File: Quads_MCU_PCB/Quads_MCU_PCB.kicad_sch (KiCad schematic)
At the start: 87 parts, among them J1 USB_C_Receptacle_USB2.0_16P, J2 Conn_01x06_Pin, J3 Conn_01x02_Pin, J4 Conn_01x03_Pin, J5 Conn_01x03_Pin, J6 Conn_01x03_Pin, J7 Conn_01x03_Pin, SW1 SW_Push, U1 STM32H723ZGTx, U3 ISOW1044, U4 TSR_1-2450, U5 AP7361C-33E, U6 ISOW1044, U7 ISOW1044, U8 MCP2518FD-xQBB, U9 ISOW1044, Y1 40MHz, Y2 25MHz

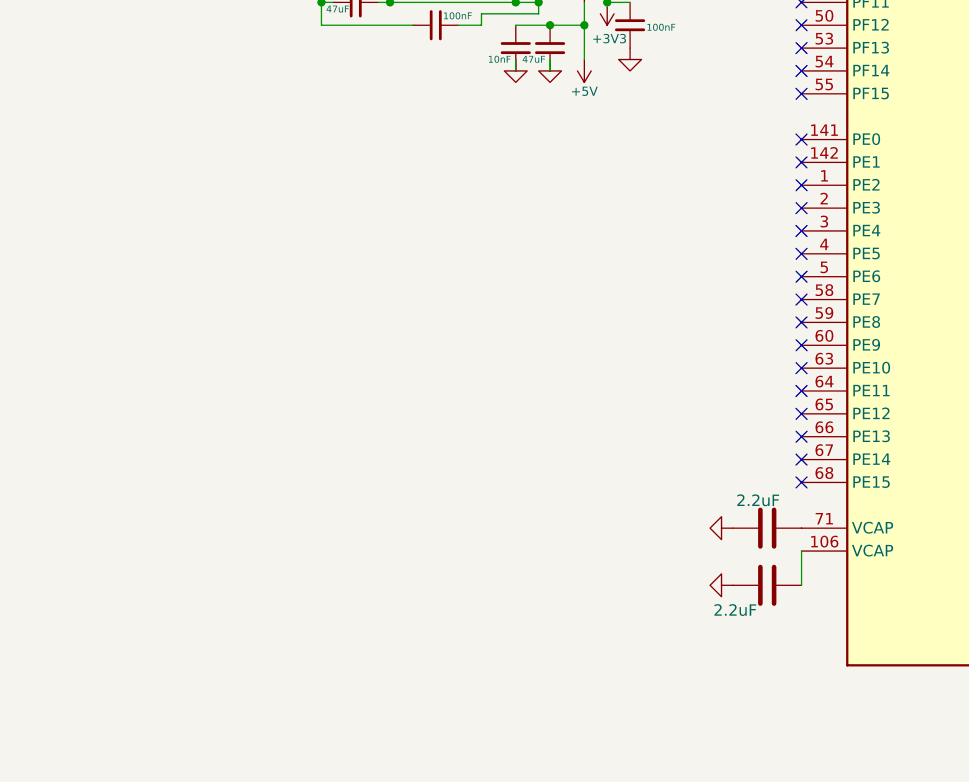
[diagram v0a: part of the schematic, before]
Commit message: Add BMI088 IMU on SPI4
U10 BMI088 (Sensor_Motion:BMI088, Bosch LGA-16) wired per datasheet
Fig. 8 (SPI mode):
- SPI4: PE2 SCK, PE5 MISO (SDO1 + SDO2), PE6 MOSI
- Chip selects as GPIO: PE3 -> CSB1 (accel), PE4 -> CSB2 (gyro)
- Data-ready interrupts: PE7 <- INT1 (accel), PE8 <- INT3 (gyro)
- PS tied to GND (selects SPI); INT2/INT4 left unconnected
- C59/C60 100nF decoupling on VDD/VDDIO, both from +3V3
- Removed the no-connect flags on PE2-PE8

SPI4 is separate from SPI1 so IMU reads don't compete with MCP2518FD
CAN traffic. ERC adds one expected pin_to_pin error: SDO1/SDO2 are both
"output" but tri-state when their CS is high, as in Bosch Fig. 8.

Co-Authored-By: Claude Opus 5.5 <noreply@anthropic.com>
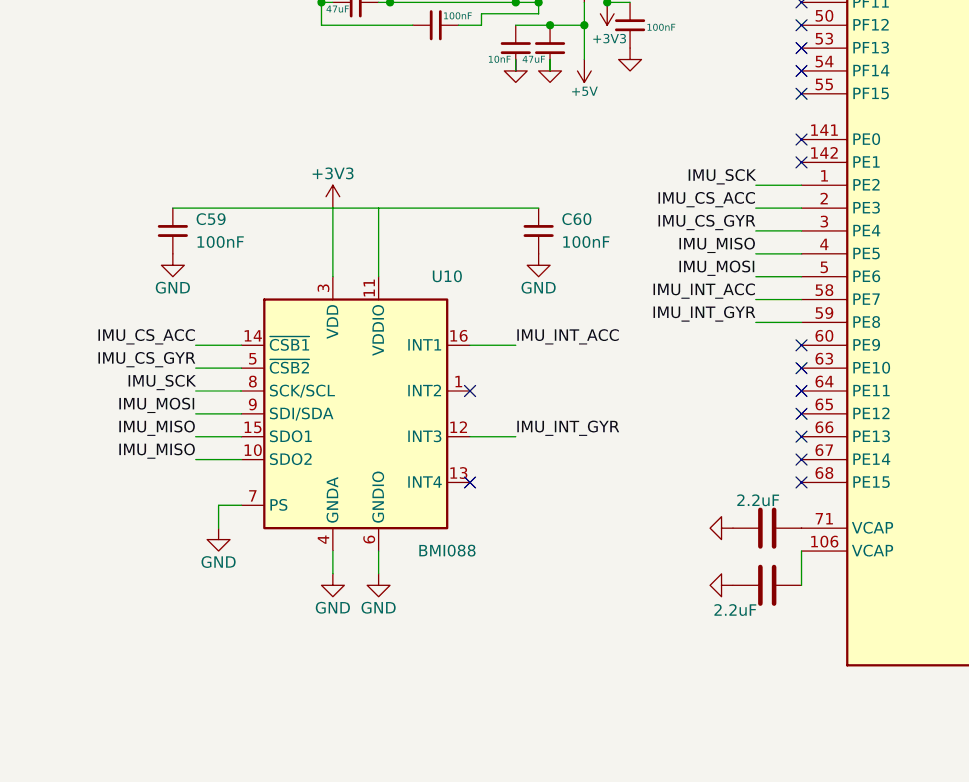
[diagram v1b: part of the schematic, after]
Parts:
- added C59, C60: 100nF, Capacitor_SMD:C_0402_1005Metric, symbol Device:C_Small
- added U10: BMI088, Package_LGA:Bosch_LGA-16_4.5x3mm_P0.5mm_LayoutBorder7x1y_ClockwisePinNumbering, symbol Sensor_Motion:BMI088
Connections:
- net +3V3: now also C59.1, C60.1, U10.11 (VDDIO), U10.3 (VDD)
- net GND: now also C59.2, C60.2, U10.2 (GNDA), U10.4 (GNDA), U10.6 (GNDIO), U10.7 (PS)
- net IMU_SCK: now reaches U1.1 (PE2)
- net IMU_SCK: now also U10.8 (SCK/SCL)
- net IMU_CS_ACC: now reaches U1.2 (PE3)
- net IMU_CS_ACC: now also U10.14 (~{CSB1})
- net IMU_CS_GYR: now reaches U1.3 (PE4)
- net IMU_CS_GYR: now also U10.5 (~{CSB2})
- net IMU_MISO: now reaches U1.4 (PE5)
- net IMU_MISO: now also U10.10 (SDO2), U10.15 (SDO1)
- net IMU_MOSI: now reaches U1.5 (PE6)
- net IMU_MOSI: now also U10.9 (SDI/SDA)
- net IMU_INT_ACC: now reaches U1.58 (PE7)
- net IMU_INT_ACC: now also U10.16 (INT1)
- net IMU_INT_GYR: now reaches U1.59 (PE8)
- net IMU_INT_GYR: now also U10.12 (INT3)
- no-connect marks 110 -> 105

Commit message: Assign footprints and LCSC part numbers for JLC assembly
0402 for small passives, 0603 for 4.7uF/10uF, 1206 for 47uF on 5V
rails, 1210 25V for C27 on +12V. Polyfuse is 1812 33V (1206 polyfuses
are only rated 6-8V). Added a hidden "LCSC" field per part; every
number was checked on jlcpcb.com (value, voltage, package,
basic/extended).

Not yet assigned:
- J2-J7 connectors (J4-J7 to become JST GH 4-pin to match ODrive S1)
- U3/U6/U7/U9 ISOW1044: out of stock at JLC
- Y1/Y2 oscillators, SW1

Netlist connectivity verified unchanged before/after.

Co-Authored-By: Claude Opus 5.5 <noreply@anthropic.com>
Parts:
- C1, C10, C11, C12, C13, C14, C15, C16, C17, C18, C20, C29, C30, C35, C36, C39, C42, C45, C49, C5, C50, C53, C57, C58, C6, C7, C8, C9: footprint (none) -> Capacitor_SMD:C_0402_1005Metric; LCSC (none) -> C1525
- C19, C4: footprint (none) -> Capacitor_SMD:C_0603_1608Metric; LCSC (none) -> C19666
- C2, C3: footprint (none) -> Capacitor_SMD:C_0402_1005Metric; LCSC (none) -> C12530
- C27: footprint (none) -> Capacitor_SMD:C_1210_3225Metric; LCSC (none) -> C90142
- C28, C32, C33, C37, C40, C43, C46, C51, C54: footprint (none) -> Capacitor_SMD:C_1206_3216Metric; LCSC (none) -> C96123
- C31, C34, C38, C41, C44, C47, C52, C55: footprint (none) -> Capacitor_SMD:C_0402_1005Metric; LCSC (none) -> C15195
- C56: footprint (none) -> Capacitor_SMD:C_0603_1608Metric; LCSC (none) -> C19702
- C59, C60: LCSC (none) -> C1525
- D1: footprint (none) -> LED_SMD:LED_0603_1608Metric; LCSC (none) -> C2286
- D2: footprint (none) -> Diode_SMD:D_SMA; LCSC (none) -> C8678
- D3: footprint (none) -> Diode_SMD:D_SMA; LCSC (none) -> C113958
- D4: footprint (none) -> Diode_SMD:D_SMA; LCSC (none) -> C364284
- F1: footprint (none) -> Fuse:Fuse_1812_4532Metric; LCSC (none) -> C21000
- J1: footprint (none) -> Connector_USB:USB_C_Receptacle_HRO_TYPE-C-31-M-12; LCSC (none) -> C165948
- R1, R2: footprint (none) -> Resistor_SMD:R_0402_1005Metric; LCSC (none) -> C25905
- R10, R11, R13, R9: footprint (none) -> Resistor_SMD:R_0402_1005Metric; LCSC (none) -> C25079
- R15, R3, R5: footprint (none) -> Resistor_SMD:R_0402_1005Metric; LCSC (none) -> C25744
- R4: footprint (none) -> Resistor_SMD:R_0402_1005Metric; LCSC (none) -> C25900
- R6: footprint (none) -> Resistor_SMD:R_0402_1005Metric; LCSC (none) -> C11702
- R7, R8: footprint (none) -> Resistor_SMD:R_0402_1005Metric; LCSC (none) -> C25092
- U1: LCSC (none) -> C730146
- U10: LCSC (none) -> C194919
- U4: LCSC (none) -> C53183920
- U5: LCSC (none) -> C500795
- U8: LCSC (none) -> C621395

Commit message: Switch CAN connectors J4-J7 to JST GH 4-pin to match ODrive S1
ODrive S1 J16/J17 is JST GH 4-pin (SM04B-GHS-TB). Pinout from the S1
datasheet: 1 = 12V IN (optional logic power), 2 = CAN_H, 3 = CAN_L,
4 = GND (not connected inside the ODrive). Matching it lets us use
straight 1:1 GH cables.

New pinout on J4-J7:
- Pin 1: NC (ODrive's 12V IN; we don't supply CAN power)
- Pin 2: CANH
- Pin 3: CANL
- Pin 4: GND2 (isolated side of the ISOW1044, so CAN stays
  galvanically isolated from the main board)

Footprint JST_GH_SM04B-GHS-TB_1x04-1MP_P1.25mm_Horizontal, LCSC
C189895. The symbol was flipped and shifted so the existing wires are
unchanged; netlist verified: only the J4-J7 pin numbers changed.

Note: ODrive requires CAN GND tied to DC- at one system star point,
since S1 CAN is referenced to DC-.

Co-Authored-By: Claude Opus 5.5 <noreply@anthropic.com>
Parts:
- J4, J5, J6, J7: value Conn_01x03_Pin -> Conn_01x04_Pin; footprint (none) -> Connector_JST:JST_GH_SM04B-GHS-TB_1x04-1MP_P1.25mm_Horizontal; symbol Connector:Conn_01x03_Pin -> Connector:Conn_01x04_Pin; LCSC (none) -> C189895
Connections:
- net at C53.1, C54.2, C55.2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: now also J4.4 (Pin_4); no longer J4.1 (Pin_1)
- net at R13.2, U9.18 (CANL): now also J4.3 (Pin_3); no longer J4.2 (Pin_2)
- net at R13.1, U9.19 (CANH): now also J4.2 (Pin_2); no longer J4.3 (Pin_3)
- net at C45.1, C46.2, C47.2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: now also J7.4 (Pin_4); no longer J7.1 (Pin_1)
- net at R11.2, U7.18 (CANL): now also J7.3 (Pin_3); no longer J7.2 (Pin_2)
- net at R11.1, U7.19 (CANH): now also J7.2 (Pin_2); no longer J7.3 (Pin_3)
- net at C31.2, C32.2, C35.1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: now also J6.4 (Pin_4); no longer J6.1 (Pin_1)
- net at R9.2, U3.18 (CANL): now also J6.3 (Pin_3); no longer J6.2 (Pin_2)
- net at R9.1, U3.19 (CANH): now also J6.2 (Pin_2); no longer J6.3 (Pin_3)
- net at C39.1, C40.2, C41.2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: now also J5.4 (Pin_4); no longer J5.1 (Pin_1)
- net at R10.2, U6.18 (CANL): now also J5.3 (Pin_3); no longer J5.2 (Pin_2)
- net at R10.1, U6.19 (CANH): now also J5.2 (Pin_2); no longer J5.3 (Pin_3)
- no-connect marks 105 -> 109

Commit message: Assign footprints for J3 power input and J2 SWD header
- J3 (12V in): Molex Micro-Fit 3.0 43045-0212, 2x01 vertical THT with
  pegs, as Advaith picked Micro-Fit 3.0. Pad 1 = 12V in, pad 2 = GND.
  LCSC C293362 (genuine Molex).
- J2 (SWD): generic 2.54mm 1x6 vertical header for now, since the
  debugger isn't chosen yet; jumpers fit any probe. LCSC C492405.

Every part now has a footprint. Still missing LCSC numbers: U3/U6/U7/U9
(ISOW1044, out of stock at JLC), Y1/Y2, SW1.

Co-Authored-By: Claude Opus 5.5 <noreply@anthropic.com>
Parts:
- J2: footprint (none) -> Connector_PinHeader_2.54mm:PinHeader_1x06_P2.54mm_Vertical; LCSC (none) -> C492405
- J3: footprint (none) -> Connector_Molex:Molex_Micro-Fit_3.0_43045-0212_2x01_P3.00mm_Vertical; LCSC (none) -> C293362

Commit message: Add LCSC part numbers for Y1, Y2 and SW1
Y1 40 MHz: C2831396 (YXC OT322540MJBA4SL)
Y2 25 MHz: C669088 (YXC OT322525MJBA4SL)
  3.3 V CMOS, 3225 4-pin, duty cycle 45-55% per datasheet
  (MCP2518FD requires 45-55% on OSC1). Pinout matches the ASE footprint.
SW1: C273528 (E-Switch TL3301NF260QG), matches the TL3301NxxxxxG footprint.
KiCad also re-sorted no_connect entries on save; no other changes.

Co-Authored-By: Claude Opus 5.5 <noreply@anthropic.com>
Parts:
- SW1: LCSC (none) -> C273528
- Y1: LCSC (none) -> C2831396
- Y2: LCSC (none) -> C669088

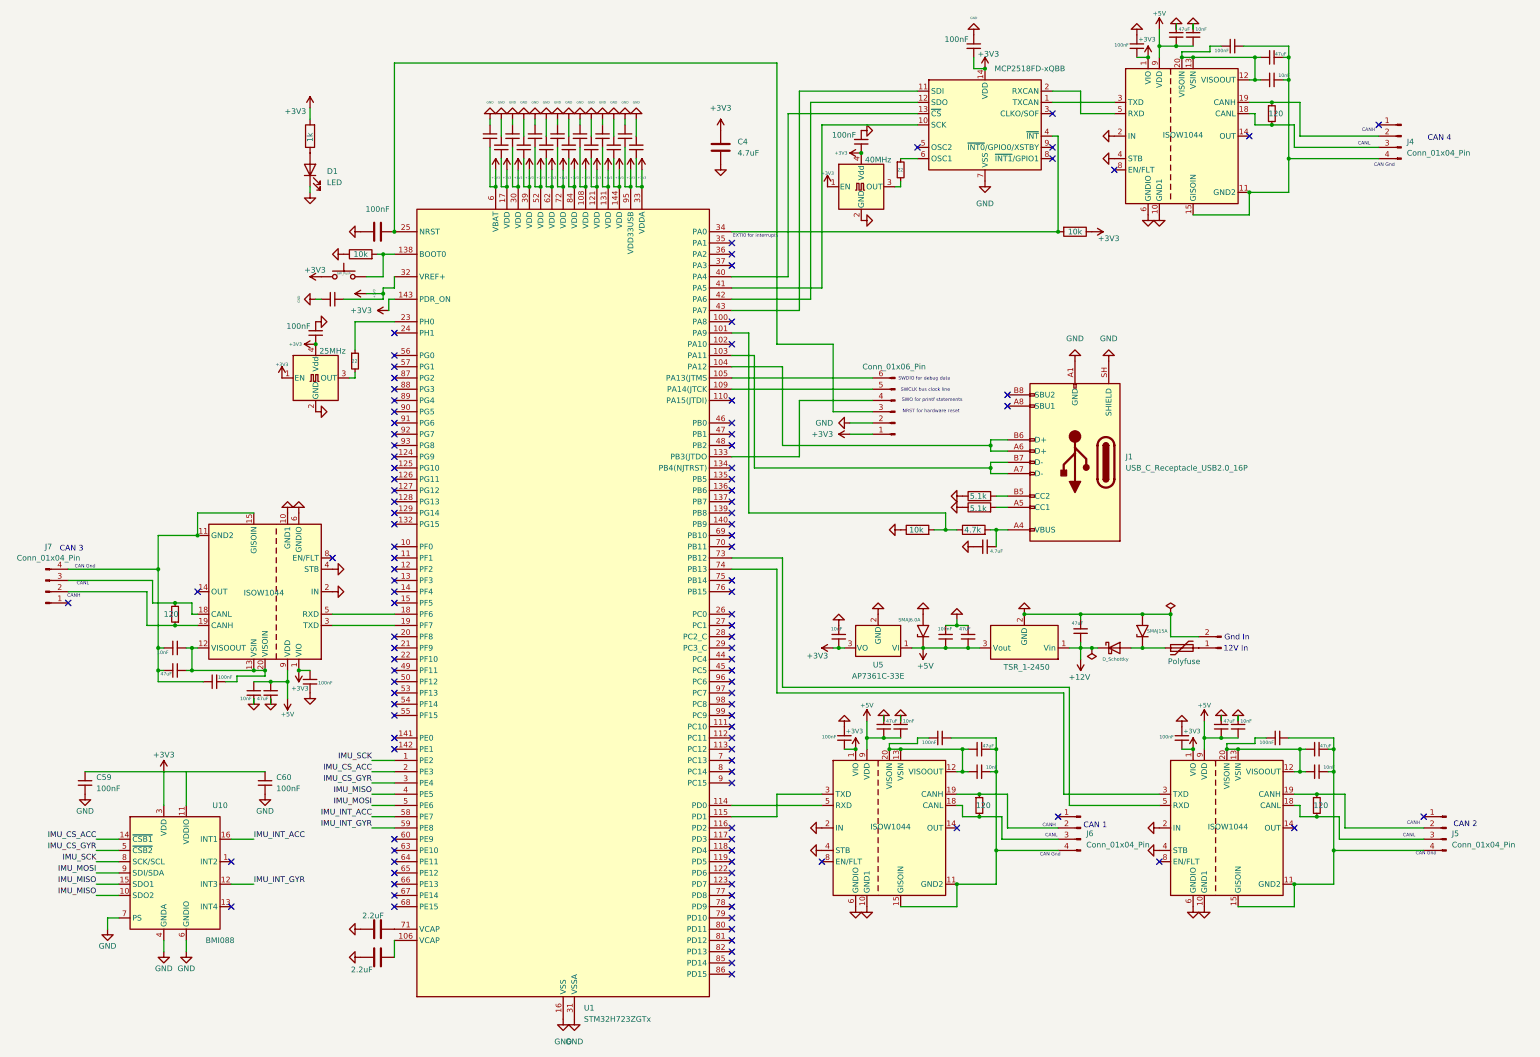
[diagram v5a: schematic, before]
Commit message: Replace out-of-stock ISOW1044 with ADM3057E on all four CAN channels
ISOW1044 is out of stock at TI until 2027. ADM3057ExRW (3 kV, SOIC-20W,
LCSC C658109) is pin-compatible enough to swap in place on U3/U6/U7/U9.

Per channel, following the ADM3055E/ADM3057E datasheet:
- SILENT, STBY, AUXIN tied to GND; AUXOUT not connected
- RS tied to GND2 (full-speed mode)
- Ferrite beads (BLM15HD182SN1D, C76888) between VISOOUT/VISOIN and
  GNDISO/GND2 to contain the 180 MHz isoPower switching noise
- Decoupling: VCC 10u+100n, VIO 100n+10n, VISOIN 100n+10n,
  VISOOUT 10u+220n returned to GNDISO (local label <U>_GNDISO)

New parts: C61-C68, FB1-FB8. Netlist checked per channel: TXD/RXD,
CANH/CANL and J pin 4 connections unchanged; ERC down to the expected
SDO1/SDO2 shared-MISO warning.

Co-Authored-By: Claude Opus 5.5 <noreply@anthropic.com>
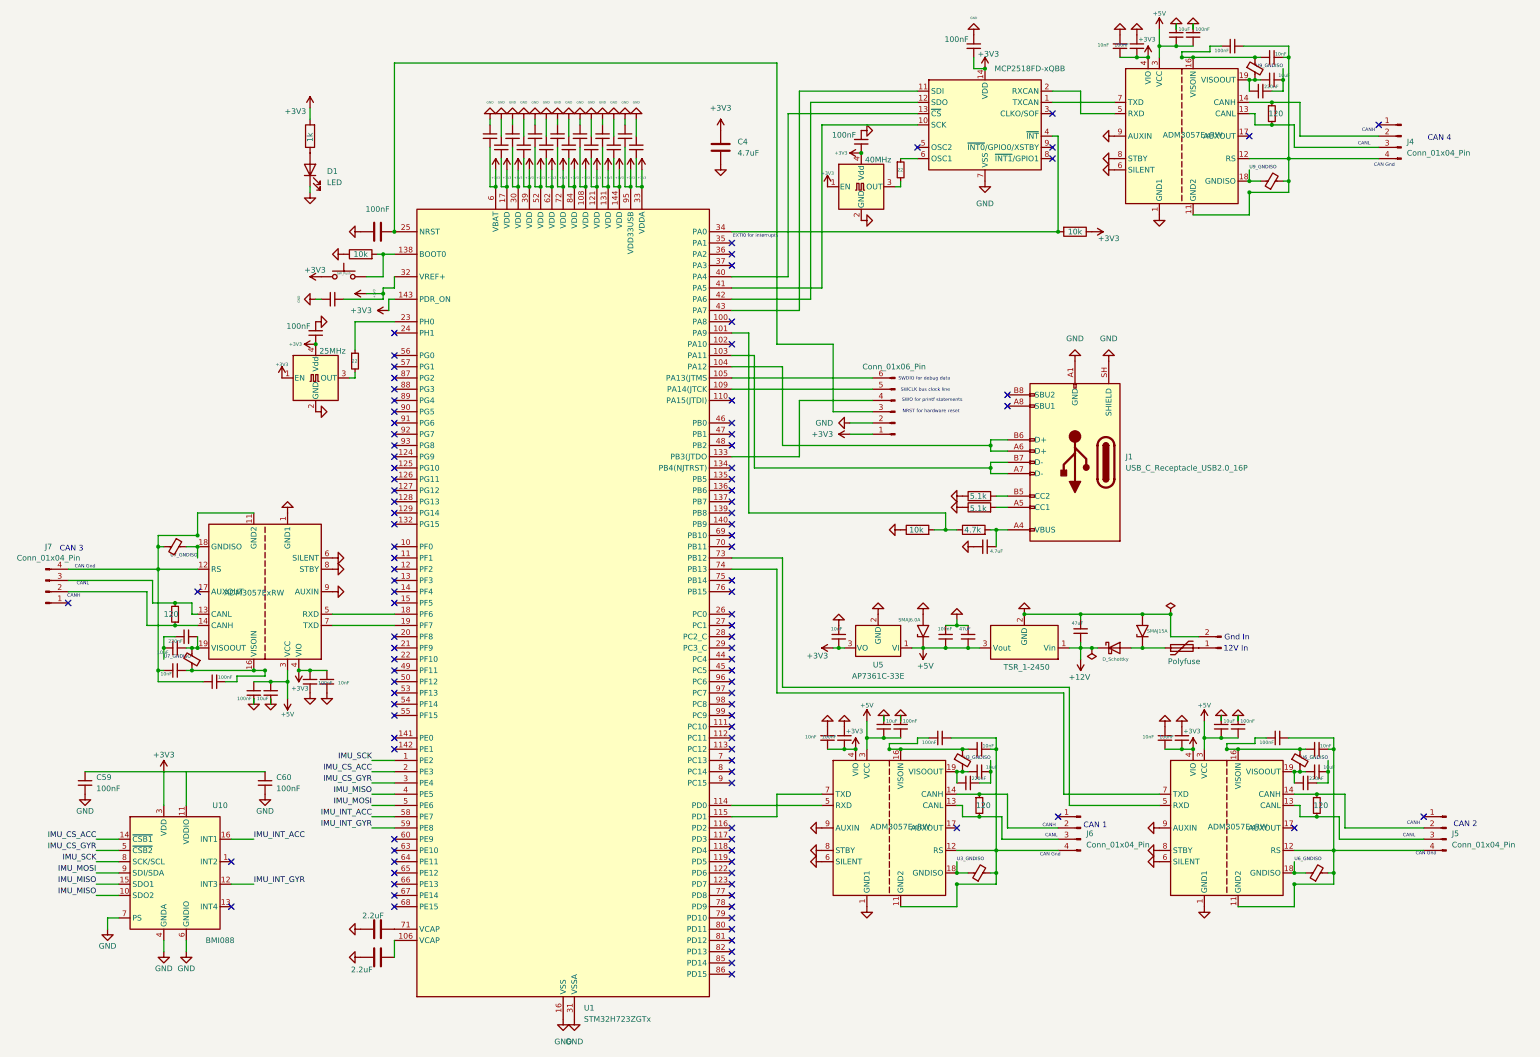
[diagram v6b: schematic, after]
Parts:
- added C61, C63, C65, C67: 10nF, Capacitor_SMD:C_0402_1005Metric, symbol Device:C_Small
- added C62, C64, C66, C68: 220nF, Capacitor_SMD:C_0402_1005Metric, symbol Device:C_Small
- added FB1, FB2, FB3, FB4, FB5, FB6, FB7, FB8: 1.8k@100MHz, Inductor_SMD:L_0402_1005Metric, symbol Device:FerriteBead_Small
- C31, C41, C47, C55: value 10nF -> 10uF; footprint Capacitor_SMD:C_0402_1005Metric -> Capacitor_SMD:C_0603_1608Metric; LCSC C15195 -> C19702
- C32, C40, C46, C54: value 47uF -> 10nF; footprint Capacitor_SMD:C_1206_3216Metric -> Capacitor_SMD:C_0402_1005Metric; LCSC C96123 -> C15195
- C33, C37, C43, C51: value 47uF -> 10uF; footprint Capacitor_SMD:C_1206_3216Metric -> Capacitor_SMD:C_0603_1608Metric; LCSC C96123 -> C19702
- C34, C38, C44, C52: value 10nF -> 100nF; LCSC C15195 -> C1525
- U3, U6, U7, U9: value ISOW1044 -> ADM3057ExRW; symbol Interface_CAN_LIN:ISOW1044 -> Interface_CAN_LIN:ADM3057ExRW; LCSC (none) -> C658109
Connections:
- net +3V3: now also U3.4 (VIO), U6.4 (VIO), U7.4 (VIO), U9.4 (VIO), C61.2, C63.2, C65.2, C67.2; no longer U3.1 (VIO), U6.1 (VIO), U7.1 (VIO), U9.1 (VIO)
- net +5V: now also U3.3 (VCC), U6.3 (VCC), U7.3 (VCC), U9.3 (VCC); no longer U3.9 (VDD), U6.9 (VDD), U7.9 (VDD), U9.9 (VDD)
- net GND: now also U3.1 (GND1), U3.8 (STBY), U3.9 (AUXIN), U6.1 (GND1), U6.8 (STBY), U6.9 (AUXIN), U7.1 (GND1), U7.8 (STBY), U7.9 (AUXIN), U9.1 (GND1), U9.8 (STBY), U9.9 (AUXIN), C61.1, C63.1, C65.1, C67.1; no longer U3.4 (STB), U6.4 (STB), U7.4 (STB), U9.4 (STB)
- net at C53.1, C54.2, J4.4 (Pin_4)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: now also U9.12 (RS), FB6.2; no longer C55.2, U9.16 (GISOIN), U9.17 (GISOIN)
- net at U9.14 (CANH): now also J4.2 (Pin_2), R13.1
- net at J4.3 (Pin_3), R13.2: now also U9.13 (CANL); no longer U9.18 (CANL)
- net at U8.1 (TXCAN): now also U9.7 (TXD); no longer U9.3 (TXD)
- net at C45.1, C46.2, J7.4 (Pin_4)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: now also U7.12 (RS), FB8.2; no longer C47.2, U7.16 (GISOIN), U7.17 (GISOIN)
- net at U7.14 (CANH): now also J7.2 (Pin_2), R11.1
- net at J7.3 (Pin_3), R11.2: now also U7.13 (CANL); no longer U7.18 (CANL)
- net at U1.19 (PF7): now also U7.7 (TXD); no longer U7.3 (TXD)
- net at C32.2, C35.1, J6.4 (Pin_4)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: now also U3.12 (RS), FB2.2; no longer C31.2, U3.16 (GISOIN), U3.17 (GISOIN)
- net at U3.14 (CANH): now also J6.2 (Pin_2), R9.1
- net at J6.3 (Pin_3), R9.2: now also U3.13 (CANL); no longer U3.18 (CANL)
- net at U1.115 (PD1): now also U3.7 (TXD); no longer U3.3 (TXD)
- net at C39.1, C40.2, J5.4 (Pin_4)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: now also U6.12 (RS), FB4.2; no longer C41.2, U6.16 (GISOIN), U6.17 (GISOIN)
- net at J5.2 (Pin_2), R10.1: now also U6.14 (CANH); no longer U6.19 (CANH)
- net at J5.3 (Pin_3), R10.2: now also U6.13 (CANL); no longer U6.18 (CANL)
- net at U1.74 (PB13): now also U6.7 (TXD); no longer U6.3 (TXD)
- new net: C45.2, C46.1, FB7.1, U7.16 (VISOIN)
- new net: C47.1, C68.1, FB7.2, U7.19 (VISOOUT)
- new net: C53.2, C54.1, FB5.1, U9.16 (VISOIN)
- new net: C55.1, C66.1, FB5.2, U9.19 (VISOOUT)
- new net: C39.2, C40.1, FB3.1, U6.16 (VISOIN)
- new net: C41.1, C64.1, FB3.2, U6.19 (VISOOUT)
- new net: C32.1, C35.2, FB1.1, U3.16 (VISOIN)
- new net: C31.1, C62.1, FB1.2, U3.19 (VISOOUT)
- new net U3_GNDISO: C31.2, C62.2, FB2.1, U3.18 (GNDISO), U3.20 (GNDISO)
- new net U6_GNDISO: C41.2, C64.2, FB4.1, U6.18 (GNDISO), U6.20 (GNDISO)
- new net U7_GNDISO: C47.2, C68.2, FB8.1, U7.18 (GNDISO), U7.20 (GNDISO)
- new net U9_GNDISO: C55.2, C66.2, FB6.1, U9.18 (GNDISO), U9.20 (GNDISO)
- no-connect marks 109 -> 105
